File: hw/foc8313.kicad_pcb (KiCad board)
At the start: 4 copper layers, 35 x 35 mm, 86 parts, among them J1 Tag Connect, J2 Aux, J3 CAN, J4 CAN, P1 USB_C_Plug, SW1 SW_SPST, SW2 SW_SPST, U1 LMR36015SFBRNXR, U12 TJA1051TK/3,118, U2 XC6206P332MR, U3 DRV8313PWP, U4 STM32F103CBTx, U5 AS5047D, U6 ZD24C08AE1-STGMT, U7 INA240A2D, U8 INA240A2D, X1 X322516MLB4SI

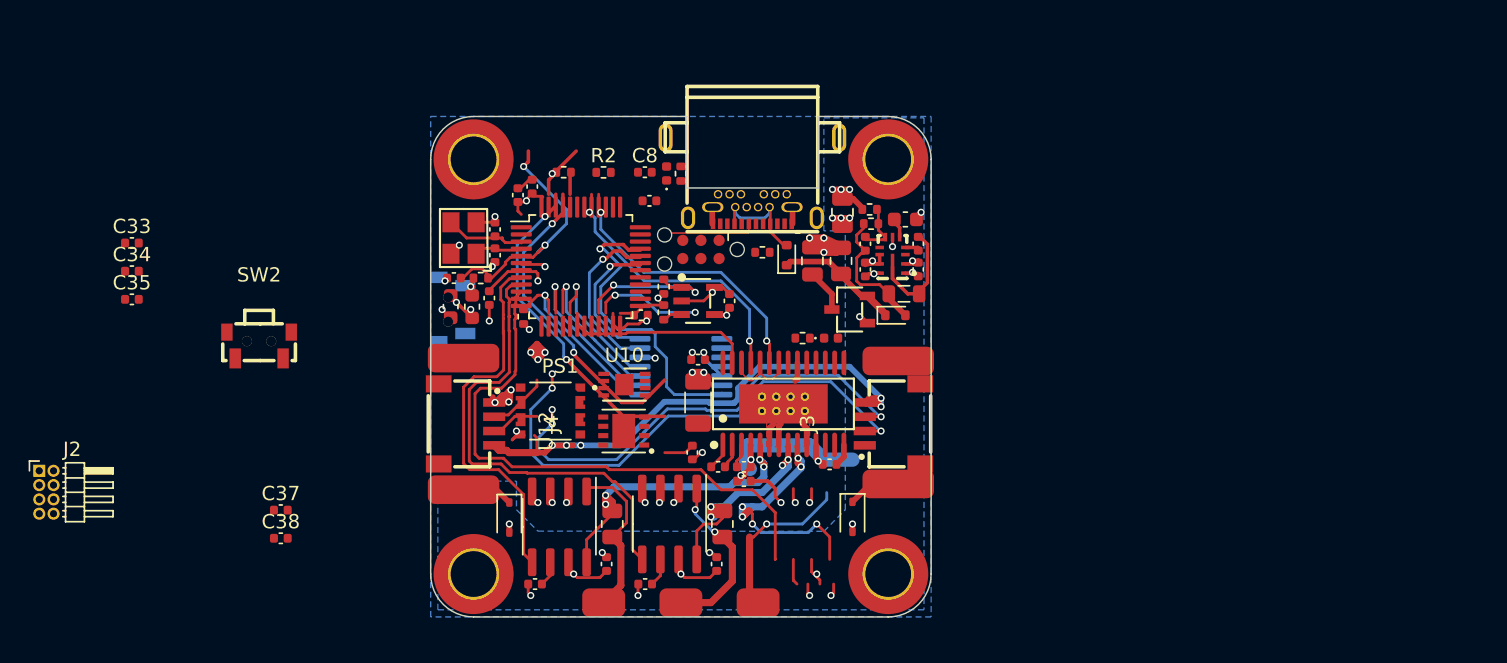
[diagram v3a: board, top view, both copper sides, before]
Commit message: [Hw] Optimised pin out for routing, new layout
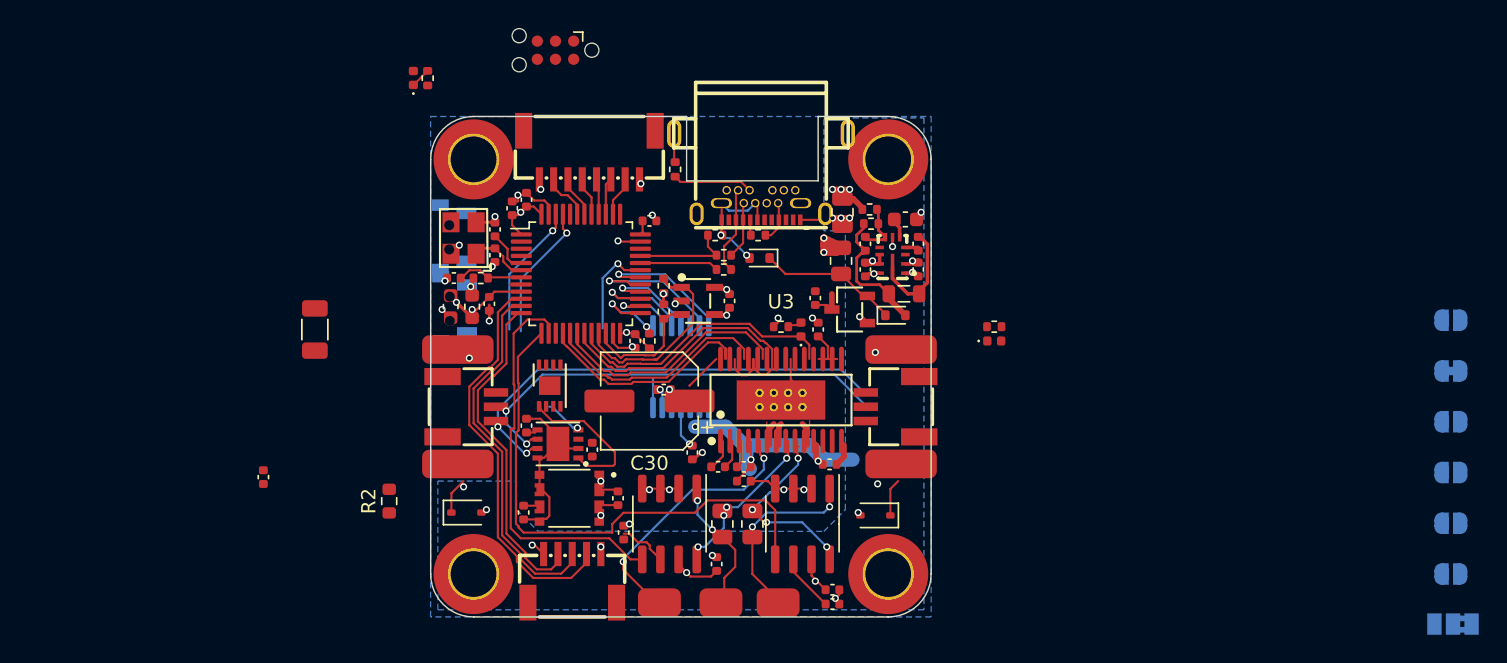
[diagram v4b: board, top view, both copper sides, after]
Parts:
- removed P1: USB_C_Plug, easyeda:USB-3.1-SMD_USB3.1-TYPE-C-FSABC
- added C30: 47u, Capacitor_SMD:CP_Elec_6.3x5.4, F.Cu at (137.8, 102.4)
- added D7: GREEN, LED_SMD:LED_0402_1005Metric, F.Cu at (161.9, 98.2)
- added J6: GPIO, easyeda:CONN-SMD_8P-P1.00_MEGASTAR_ZX-SH1.0-8PWT, F.Cu at (133.6, 85.2)
- added JP1: *, Jumper:SolderJumper-3_P1.3mm_Bridged2Bar12_Pad1.0x1.5mm, B.Cu at (194.0, 118.0)
- added JP2: *, Jumper:SolderJumper-2_P1.3mm_Open_RoundedPad1.0x1.5mm, B.Cu at (193.8, 96.8)
- added JP3: *, Jumper:SolderJumper-2_P1.3mm_Bridged_RoundedPad1.0x1.5mm, B.Cu at (193.8, 100.3)
- added JP4: *, Jumper:SolderJumper-2_P1.3mm_Open_RoundedPad1.0x1.5mm, B.Cu at (193.8, 103.8)
- added JP5: *, Jumper:SolderJumper-2_P1.3mm_Open_RoundedPad1.0x1.5mm, B.Cu at (193.8, 107.4)
- added JP6: *, Jumper:SolderJumper-2_P1.3mm_Open_RoundedPad1.0x1.5mm, B.Cu at (193.8, 111.0)
- added JP7: *, Jumper:SolderJumper-2_P1.3mm_Open_RoundedPad1.0x1.5mm, B.Cu at (193.8, 114.5)
- added R14: 5.1k, Resistor_SMD:R_0402_1005Metric, F.Cu at (145.4, 90.8)
- added R15: 5.1k, Resistor_SMD:R_0402_1005Metric, F.Cu at (139.6, 86.2)
- added R16: 22, Resistor_SMD:R_0402_1005Metric, F.Cu at (143.0, 93.2)
- added R17: 1k5, Resistor_SMD:R_0402_1005Metric, F.Cu at (142.4, 90.8)
- added USB1: USB3.1-TYPE-C-FSABC, easyeda:USB-3.1-SMD_USB3.1-TYPE-C-FSABC, F.Cu at (145.6, 86.7)
- C18: footprint Capacitor_SMD:C_0805_2012Metric -> Capacitor_SMD:C_0402_1005Metric
- C8: value 100n -> 470n
- J2: value Aux -> Encoder; footprint Connector_PinHeader_1.00mm:PinHeader_2x04_P1.00mm_Horizontal -> easyeda:CONN-SMD_5P-P1.00_MEGASTAR_ZX-SH1.0-5PWT
- J3, J4: footprint easyeda:CONN-SMD_4P-P1.00_INCP_IPCW100W14XXXXR -> easyeda:CONN-SMD_AFC10-S03QCA-00
- R11: value 5.1k -> 22
- R2: value 100k -> 120; footprint Resistor_SMD:R_0402_1005Metric -> Resistor_SMD:R_0603_1608Metric
- R5: value 1k5 -> 10k
- R7: value 100k -> 20k
- SW2: moved to B.Cu
- moved J2 38.0 mm to (132.4, 114.8)
- moved C33 35.3 mm to (133.8, 105.8), turned to -90 degrees
- moved R7 32.9 mm to (161.9, 97.2), turned to 0 degrees
- moved C34 29.6 mm to (129.2, 104.1), turned to 90 degrees
- moved R2 27.4 mm to (119.6, 109.4), turned to 90 degrees
- moved C19 27.3 mm to (114.4, 97.4)
- moved C37 23.6 mm to (135.6, 109.2), turned to 90 degrees
- moved C26 20.8 mm to (150.6, 116.6), turned to 0 degrees
- moved R8 18.9 mm to (122.3, 79.8)
- moved D5 18.9 mm to (121.3, 79.8)
- moved J1 17.3 mm to (131.2, 77.9)
- moved C38 17.1 mm to (129.0, 110.2), turned to -90 degrees
- moved U7 17.0 mm to (148.5, 111.0)
- moved C8 16.4 mm to (149.6, 97.4), turned to 90 degrees
- moved C27 15.9 mm to (150.6, 115.6), turned to 0 degrees
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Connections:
- net /ENC_Z renamed /ENC1_Z
- net /PHA renamed /PHC
- net Net-(U10-INB) renamed /isocan/ISORX
- net Net-(U10-OUTA) renamed /isocan/ISOTX
- C22 pad 1: Net-(U3-VCP) -> VCC
- C22 pad 2: VCC -> Net-(U3-VCP)
- C24 pad 1: +3V3 -> Net-(U5-VDD3V3)
- C34 pad 1: /isocan/ISO5V -> /isocan/ISOVIO
- C37 pad 1: /isocan/5V -> +5V
- C8 pad 1: /~{BTN} -> /~{DRV_NRST}
- D6 pad 2: Net-(D6-A) -> +5VD
- J2 pad 1: unconnected-(J2-Pin_1-Pad1) -> GND
- J2 pad 2: unconnected-(J2-Pin_2-Pad2) -> /ENC2_Z
- J2 pad 3: unconnected-(J2-Pin_3-Pad3) -> /ENC2_B
- J2 pad 4: unconnected-(J2-Pin_4-Pad4) -> /ENC2_A
- J2 pad 5: unconnected-(J2-Pin_5-Pad5) -> +5V
- J2 pad 6: unconnected-(J2-Pin_6-Pad6) -> (no net)
- J2 pad 7: unconnected-(J2-Pin_7-Pad7) -> (no net)
- J3 pad 1: /CAN.V- -> /CAN.GND
- J3 pad 4: /CAN.V+ -> (no net)
- J4 pad 1: /CAN.V- -> /CAN.GND
- J4 pad 4: /CAN.V+ -> (no net)
- PS1 pad 8: /isocan/5V -> +5V
- PS1 pad 9_10: /isocan/5V -> +5V
- R10 pad 2: /I2C.SCL -> /I2C2.SDA
- R11 pad 1: Net-(P1-CC) -> /USB_DP
- R11 pad 2: GND -> /USB_DP_EXT
- R12 pad 2: /OUTA -> /OUTC
- R2 pad 1: +3.3V -> /CAN.H
- R2 pad 2: /~{BTN} -> /CAN.L
- R5 pad 1: GND -> /~{SPI2_NSS}
- R5 pad 2: Net-(U4-BOOT0) -> +3.3V
- R7 pad 1: +3V3 -> VCC
- R7 pad 2: /~{SPI1_NSS} -> Net-(D7-A)
- R9 pad 2: /I2C.SDA -> /I2C2.SCL
- U12 pad 5: /isocan/ISO5V -> /isocan/ISOVIO
- U3 pad 15: unconnected-(U3-V3P3-Pad15) -> /~{DRV_NRST}
- U3 pad 17: /~{DRV_NSLEEP} -> /~{DRV_NRST}
- U3 pad 23: /DRV_INA -> /DRV_INC
- U3 pad 27: /DRV_INC -> /DRV_INA
- U3 pad 5: /OUTC -> /OUTA
- U4 pad 10: /ISENSE_A -> /ENC2_A
- U4 pad 11: /ISENSE_B -> /ENC2_B
- U4 pad 12: /ISENSE_C -> /ENC2_Z
- U4 pad 13: unconnected-(U4-PA3-Pad13) -> /ISENSE_C
- U4 pad 14: /~{SPI1_NSS} -> /ISENSE_B
- U4 pad 15: /SPI1_SCLK -> /STATUS
- U4 pad 16: /SPI1_MISO -> /DRV_INA
- U4 pad 17: /SPI1_MOSI -> /DRV_INB
- U4 pad 19: unconnected-(U4-PB1-Pad19) -> /DRV_EN
- U4 pad 2: unconnected-(U4-PC13-Pad2) -> /~{BTN}
- U4 pad 20: unconnected-(U4-PB2-Pad20) -> /~{DRV_NFAULT}
- U4 pad 21: /I2C.SCL -> /I2C2.SCL
- U4 pad 22: /I2C.SDA -> /I2C2.SDA
- U4 pad 25: /DRV_EN -> /~{SPI2_NSS}
- U4 pad 26: unconnected-(U4-PB13-Pad26) -> /SPI2_SCK
- U4 pad 27: unconnected-(U4-PB14-Pad27) -> /SPI2_MISO
- U4 pad 28: unconnected-(U4-PB15-Pad28) -> /SPI2_MOSI
- U4 pad 29: /ENC_A -> /ENC1_B
- U4 pad 3: /~{DRV_NFAULT} -> unconnected-(U4-PC14-Pad3)
- U4 pad 30: /ENC_B -> /ENC1_A
- U4 pad 38: /STATUS -> /GPIO4
- U4 pad 39: unconnected-(U4-PB3-Pad39) -> /GPIO3
- U4 pad 40: /DRV_INA -> /GPIO2
- U4 pad 41: /DRV_INB -> /GPIO1
- U4 pad 42: unconnected-(U4-PB6-Pad42) -> /COM2
- U4 pad 43: unconnected-(U4-PB7-Pad43) -> /COM1
- U4 pad 44: Net-(U4-BOOT0) -> /BOOT0
- U5 pad 1: /~{SPI1_NSS} -> /~{SPI2_NSS}
- U5 pad 11: +3V3 -> +3.3V
- U5 pad 12: +3V3 -> Net-(U5-VDD3V3)
- U5 pad 2: /SPI1_SCLK -> /SPI2_SCK
- U5 pad 3: /SPI1_MISO -> /SPI2_MISO
- U5 pad 4: /SPI1_MOSI -> /SPI2_MOSI
- U5 pad 6: /ENC_B -> /ENC1_B
- U5 pad 7: /ENC_A -> /ENC1_A
- U6 pad 1: /I2C.SCL -> /I2C2.SCL
- U6 pad 3: /I2C.SDA -> /I2C2.SDA
- U7 pad 1: /OUTA -> /OUTC
- U7 pad 5: /ISENSE_A -> /ISENSE_C
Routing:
- net /CAN.V+: track 37.1 -> 0.00 mm, vias 5 -> 0
- net /ENC2_A: track 0.00 -> 28.1 mm
- net /ISENSE_A: track 26.8 -> 0.00 mm
- net /PHC: track 39.3 -> 12.6 mm, vias 9 -> 4
- net /ENC2_B: track 0.00 -> 25.9 mm
- net /ENC2_Z: track 0.00 -> 23.4 mm
- net /~{DRV_NFAULT}: track 0.00 -> 19.5 mm
- net /DRV_EN: track 5.50 -> 23.2 mm
- net /I2C2.SCL: track 0.00 -> 13.7 mm
- net /~{SPI1_NSS}: track 13.4 -> 0.00 mm, vias 1 -> 0
- net /CAN.TX: track 22.7 -> 9.41 mm, vias 2 -> 1
- net /ENC1_Z: track 21.6 -> 8.77 mm
- net /CAN.RX: track 22.2 -> 9.56 mm, vias 2 -> 1
- net /ENC_B: track 11.9 -> 0.00 mm, vias 1 -> 0
- net /SPI1_SCLK: track 11.7 -> 0.00 mm, vias 1 -> 0
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- added copper zone on In1.Cu, net /CAN.GND
- added copper zone on In2.Cu, net /CAN.GND
- removed copper zone on In1.Cu, net /CAN.V-
- removed copper zone on In2.Cu, net /CAN.V-
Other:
- outline, holes or cut-outs redrawn

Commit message: [Hw] Routing topology complete
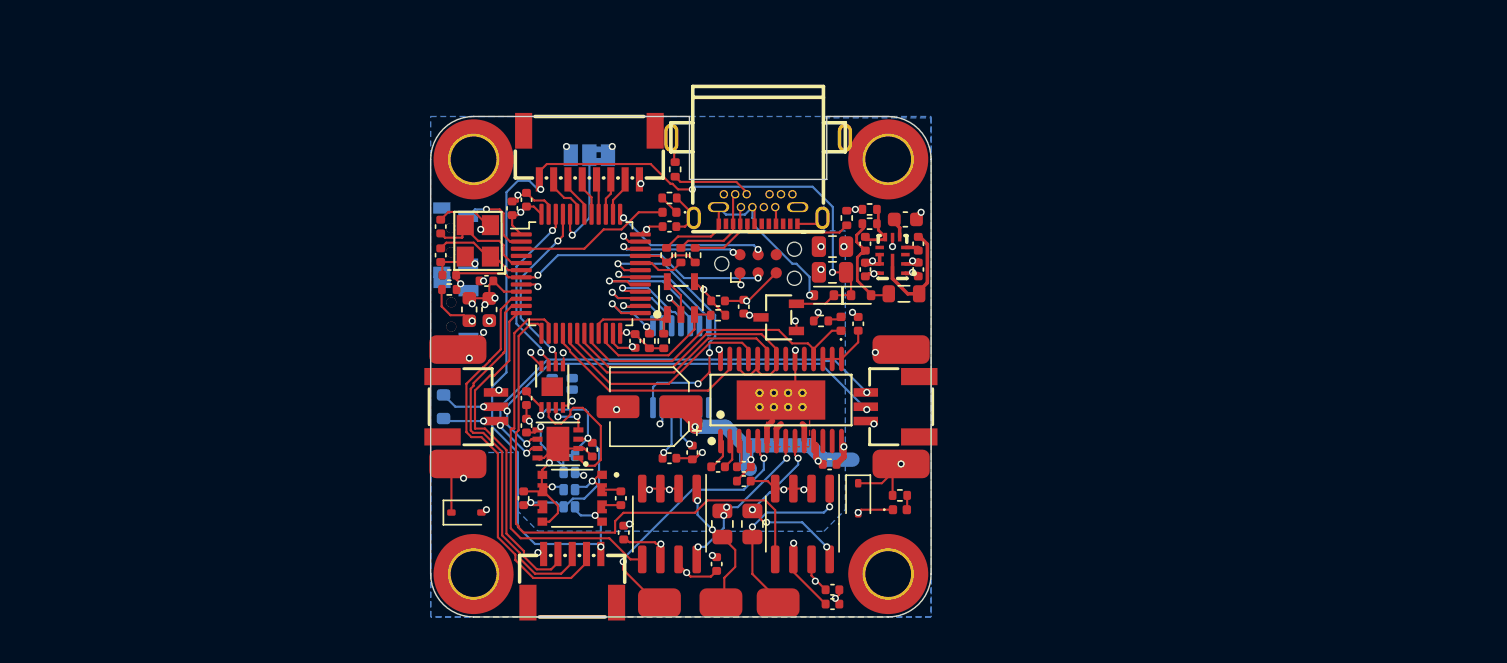
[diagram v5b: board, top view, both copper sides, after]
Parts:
- removed C19: 10u, Capacitor_SMD:C_1206_3216Metric
- C14: footprint Resistor_SMD:R_0805_2012Metric -> Capacitor_SMD:C_0805_2012Metric
- C30: footprint Capacitor_SMD:CP_Elec_6.3x5.4 -> Capacitor_SMD:CP_Elec_5x5.7
- H1, H2, H3, H4: footprint local_lib:2x5 -> local_lib:2x4
- JP2, JP4, JP5, JP6, JP7: footprint Jumper:SolderJumper-2_P1.3mm_Open_RoundedPad1.0x1.5mm -> local_lib:jumper12_open
- JP3: footprint Jumper:SolderJumper-2_P1.3mm_Bridged_RoundedPad1.0x1.5mm -> local_lib:jumper12_closed
- R2: moved to B.Cu
- moved JP1 68.7 mm to (133.6, 85.2)
- moved JP6 63.6 mm to (131.0, 101.2), turned to -90 degrees
- moved JP7 62.9 mm to (132.4, 101.2), turned to -90 degrees
- moved JP2 62.8 mm to (132.2, 108.6)
- moved JP4 61.9 mm to (132.2, 109.8)
- moved JP3 61.9 mm to (132.2, 106.2), turned to 0 degrees
- moved JP5 61.7 mm to (132.2, 107.4)
- moved J1 20.6 mm to (145.4, 92.8), turned to 0 degrees
- moved D5 20.2 mm to (139.2, 89.2), turned to 180 degrees
- moved C35 19.2 mm to (129.2, 102.2), turned to -90 degrees
- moved R8 18.9 mm to (139.2, 88.2), turned to 0 degrees
- moved D7 13.5 mm to (155.3, 110.0)
- moved R7 13.5 mm to (155.3, 109.0)
- moved R2 7.62 mm to (123.4, 102.8)
- moved R14 6.32 mm to (151.6, 89.6), turned to 90 degrees
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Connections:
- SW1 pad 1: /~{NRST} -> /~{BTN}
- SW2 pad 1: /~{BTN} -> /~{NRST}
- U4 pad 15: /STATUS -> unconnected-(U4-PA5-Pad15)
- U4 pad 3: unconnected-(U4-PC14-Pad3) -> /STATUS
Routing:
- net +5V: track 12.3 -> 75.2 mm, vias 3 -> 5
- net /~{NRST}: track 4.71 -> 24.6 mm, vias 0 -> 3
- net /isocan/ISO5V: track 1.12 -> 20.8 mm, vias 0 -> 3
- net /ENC1_Z: track 8.77 -> 20.1 mm, vias 1 -> 3
- net /SWCLK: track 0.00 -> 11.0 mm, vias 0 -> 2
- net /STATUS: track 0.00 -> 10.9 mm
- net /SWDIO: track 0.00 -> 9.59 mm, vias 0 -> 2
- net +5VD: track 8.52 -> 17.7 mm, vias 2 -> 1
- net GND: track 60.9 -> 69.9 mm, vias 39 -> 42
- net +3.3V: track 25.0 -> 32.9 mm, vias 7 -> 13
- net /BOOT0: track 0.00 -> 7.59 mm, vias 0 -> 1
- net Net-(USB1-CC1): track 1.13 -> 7.72 mm
- net /I2C2.SCL: track 13.7 -> 7.17 mm
- net /~{BTN}: track 0.00 -> 5.74 mm, vias 0 -> 1
- net /isocan/ISOVIO: track 0.84 -> 6.35 mm, vias 0 -> 1
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- added copper zone on In2.Cu, net +3.3V
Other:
- outline, holes or cut-outs redrawn

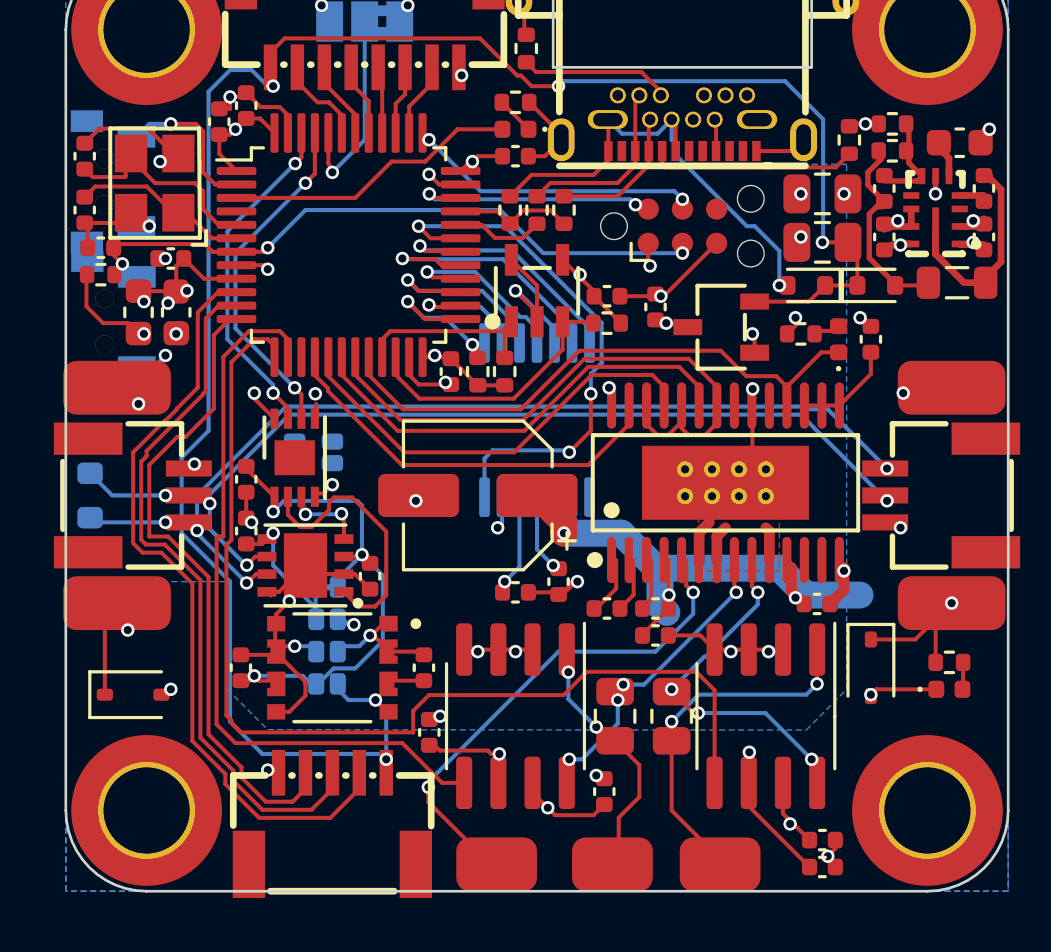
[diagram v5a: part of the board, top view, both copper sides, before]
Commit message: [Hw] Untangled isolation jumpers
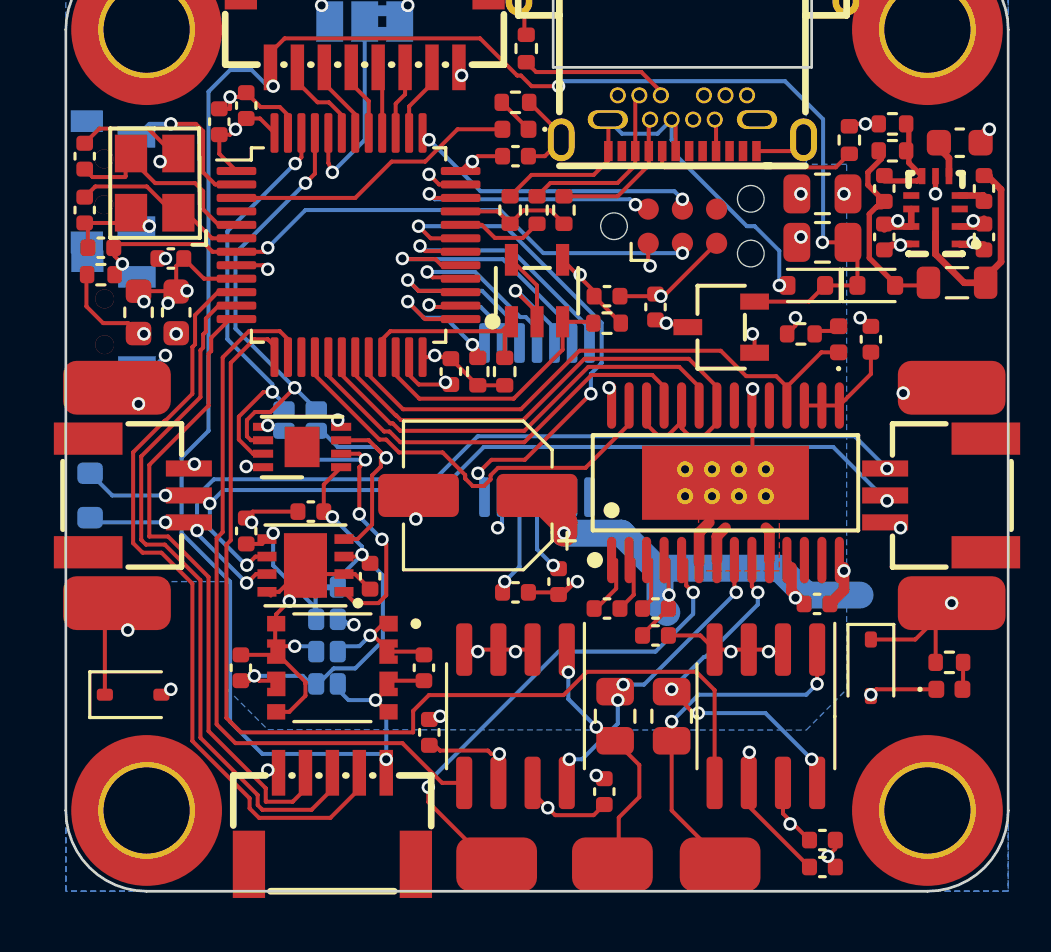
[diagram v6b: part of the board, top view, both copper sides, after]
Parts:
- moved C35 2.68 mm to (131.6, 103.4), turned to 180 degrees
- moved JP7 1.34 mm to (131.8, 100.0)
- moved JP6 1.26 mm to (130.6, 100.0)
- moved U10 0.49 mm to (131.3, 101.0), turned to 180 degrees
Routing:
- net /isocan/ISORX: track 3.04 -> 8.84 mm, vias 2 -> 1
- net /CAN.RX: track 12.8 -> 16.5 mm
- net /isocan/ISO5V: track 20.8 -> 17.3 mm
- net /CAN.TX: track 12.7 -> 15.9 mm
- net /isocan/ISOTX: track 9.98 -> 11.9 mm, vias 0 -> 3
- net /CAN.L: track 35.1 -> 33.9 mm
- net /CAN.H: track 36.1 -> 35.2 mm
- net /ENC1_Z: track 20.1 -> 19.2 mm
- net +3.3V: track 32.9 -> 32.2 mm
- net /DRV_INA: track 15.1 -> 15.9 mm
